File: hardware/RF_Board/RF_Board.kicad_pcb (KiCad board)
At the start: 4 copper layers, 90 x 90 mm, 130 parts, among them J1 Conn_Coaxial, J2 Conn_01x04_Male, J3 Conn_Coaxial, J4 Conn_01x04_Male, J5 Conn_01x06_Female, J6 Conn_01x06_Female, J7 Conn_01x06_Female, J8 L77TSAH15SOL2RM8, Q1 2N7002, Q2 2N7002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

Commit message: Finish RF board routing
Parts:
- removed R24, R25, R26, R27, R28, R29: 0, RF_Board_Footprints:R_0603_1608Metric
- added J9: Conn_01x09_Male, RF_Board_Footprints:PinHeader_1x09_P2.54mm_Vertical, F.Cu at (36.9, 22.6)
- D1, D7: footprint RF_Board_Footprints:D_SMB_Handsoldering -> RF_Board_Footprints:SOD882
- D2, D8: footprint RF_Board_Footprints:D_SMB_Handsoldering -> RF_Board_Footprints:D_SOD-523
- Q1, Q2: footprint RF_Board_Footprints:SOT-23-3 -> Package_TO_SOT_SMD:SOT-23
- moved D8 115.5 mm to (37.5, 54.4)
- moved D1 114.4 mm to (49.9, 57.9)
- moved D7 89.6 mm to (39.9, 57.9)
- moved D2 86.3 mm to (47.4, 54.4)
- moved R6 6.91 mm to (32.9, 50.8), turned to 180 degrees
- moved R7 5.76 mm to (42.8, 50.8), turned to 180 degrees
- moved R16 4.77 mm to (64.9, 62.3), turned to -90 degrees
- moved Q1 4.16 mm to (68.0, 63.1), turned to 180 degrees
- moved D5 2.00 mm to (67.5, 60.3), turned to 180 degrees
- moved R22 1.46 mm to (34.3, 59.1)
- moved C53 1.33 mm to (37.8, 52.7)
- moved C50 1.04 mm to (47.7, 52.7)
- moved D6 0.99 mm to (7.33, 76.0)
- moved Q2 0.99 mm to (6.99, 73.0)
- moved R17 0.99 mm to (9.88, 74.0)
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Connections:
- U10 pad 9: (no net) -> GND
- U11 pad 9: (no net) -> GND
- U14 pad V: (no net) -> GND
- U15 pad V: (no net) -> GND
- U2 pad 1: /CC2500_RX_EMPTY -> /CC2500_TX_EMPTY
- U2 pad 2: /CC2500_TX_OVERFLOW -> /CC2500_RX_OVERFLOW
- U2 pad 3: /CC2500_RX_OVERFLOW -> /CC2500_TX_OVERFLOW
- U2 pad 48: /CC2500_TX_EMPTY -> /CC2500_RX_EMPTY
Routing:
- net /RFM_AUX_RST: track 0.00 -> 74.9 mm, vias 0 -> 1
- net /RFM_AUX_CSN: track 0.00 -> 73.9 mm, vias 0 -> 1
- net /RFM_AUX_DIO0: track 0.00 -> 66.7 mm, vias 0 -> 2
- net /CC2500_CSN: track 24.7 -> 84.2 mm, vias 0 -> 1
- net /GDO0: track 38.5 -> 95.1 mm, vias 0 -> 1
- net /GDO2: track 41.0 -> 95.4 mm, vias 2 -> 3
- net /PA_EN: track 2.44 -> 55.1 mm, vias 1 -> 2
- net /CC2500_MOSI: track 36.0 -> 87.8 mm, vias 2 -> 3
- net /CC2500_MISO: track 31.4 -> 79.6 mm, vias 2 -> 3
- net /PA_VDET: track 6.22 -> 53.2 mm, vias 1 -> 2
- net /CC2500_SCLK: track 34.4 -> 80.4 mm, vias 2 -> 3
- net /3V3_IN: track 0.00 -> 25.6 mm
- net Net-(H3-Pad1): track 0.00 -> 6.68 mm
- net Net-(H2-Pad1): track 0.00 -> 6.68 mm
- net Net-(H4-Pad1): track 0.00 -> 6.67 mm
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- added copper zone on F.Cu, net +3.3V
- added copper zone on In2.Cu, net +3.3V
- added copper zone on F.Cu, net +5V
- added copper zone on In2.Cu, net +5V
- added copper zone on F.Cu, net /3V3_IN
- added copper zone on F.Cu, net /5V0_IN
- added copper zone on B.Cu, net GND
- added copper zone on F.Cu, net GND
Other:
- board text added: "0"
- board text added: "1"
- board text added: "2"
- board text added: "3"
- board text added: "4"
- board text added: "5"
- board text added: "5V"
- board text added: "CSN"
- board text added: "DIO"
- board text added: "GDO0"
- board text added: "GDO2"
- board text added: "MISO"
- board text added: "MOSI"
- board text added: "R'Sat RF Board Rev. 1 Merrick Slane - 2023"
- board text added: "RST"
- board text added: "SBAND"
- board text added: "SBAND ACTY"
- board text added: "SCK"
- board text added: "UHF ACTY"
- board text added: "U_CSN"
- board text added: "U_DIO0"
- board text added: "U_RST"

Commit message: more RF board touch-ups
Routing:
- net +3.3V: vias 17 -> 16
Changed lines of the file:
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@@
   (gr_line (start 88 21) (end 87 21) (layer "B.SilkS") (width 0.15))
   (gr_line (start 88 31) (end 87 31) (layer "B.SilkS") (width 0.15))
+  (gr_line (start 29.718 59.966) (end 29.718 64.03) (layer "F.SilkS") (width 0.15))
+  (gr_line (start 29.718 65.024) (end 29.718 69.088) (layer "F.SilkS") (width 0.15))
   (gr_arc (start 87.46 0) (mid 89.256051 0.743949) (end 90 2.54) (layer "Edge.Cuts") (width 0.2))
   (gr_line (start 87.46 90) (end 2.54 90) (layer "Edge.Cuts") (width 0.2))
@@
   (gr_line (start 2.54 0) (end 87.46 0) (layer "Edge.Cuts") (width 0.2))
   (gr_arc (start 0 2.54) (mid 0.743949 0.743949) (end 2.54 0) (layer "Edge.Cuts") (width 0.2))
+  (gr_text "5V" (at 30.734 67.056 90) (layer "F.SilkS")
+    (effects (font (size 1 1) (thickness 0.2)))
+  )
   (gr_text "SCK" (at 2.032 30.248) (layer "F.SilkS")
     (effects (font (size 1 1) (thickness 0.2)))
@@
     (effects (font (size 1 1) (thickness 0.15)))
   )
+  (gr_text "GND" (at 30.734 61.998 90) (layer "F.SilkS")
+    (effects (font (size 1 1) (thickness 0.2)))
+  )
   (gr_text "U_DIO0" (at 41.529 27.708) (layer "F.SilkS")
     (effects (font (size 1 1) (thickness 0.2)))
@@
     (effects (font (size 1 1) (thickness 0.2)))
   )
-  (segment (start 56.358 49.7078) (end 56.358 48.498) (width 0.3302) (layer "F.Cu") (net 1))
   (segment (start 55.358 47.498) (end 53.467 47.498) (width 0.3302) (layer "F.Cu") (net 1))
   (segment (start 53.058 47.498) (end 53.467 47.498) (width 0.62) (layer "F.Cu") (net 1))
+  (segment (start 56.358 49.7078) (end 56.358 48.498) (width 0.4318) (layer "F.Cu") (net 1))
   (arc (start 56.358 48.498) (mid 56.065107 47.790893) (end 55.358 47.498) (width 0.3302) (layer "F.Cu") (net 1))
   (segment (start 50.2252 47.498) (end 51.562 47.498) (width 0.3302) (layer "F.Cu") (net 2))
@@
   (arc (start 50.2252 47.498) (mid 49.518093 47.205107) (end 49.2252 46.498) (width 0.3302) (layer "F.Cu") (net 2))
   (segment (start 68.834 42.87) (end 68.834 43.434) (width 0.62) (layer "F.Cu") (net 3))
-  (segment (start 58.307998 49.7078) (end 58.307998 48.228) (width 0.3302) (layer "F.Cu") (net 3))
+  (segment (start 58.307998 49.7078) (end 58.307998 48.228) (width 0.4318) (layer "F.Cu") (net 3))
   (segment (start 60.307998 46.228) (end 66.834 46.228) (width 0.3302) (layer "F.Cu") (net 3))
   (segment (start 68.834 44.228) (end 68.834 43.434) (width 0.3302) (layer "F.Cu") (net 3))
@@
   (via (at 55.109 36.957) (size 0.508) (drill 0.254) (layers "F.Cu" "B.Cu") (net 14))
   (via (at 15.876 14.478) (size 1) (drill 0.5) (layers "F.Cu" "B.Cu") (net 14))
-  (via (at 36.83 52.705) (size 0.508) (drill 0.254) (layers "F.Cu" "B.Cu") (net 14))
+  (via (at 36.83 52.705) (size 1) (drill 0.5) (layers "F.Cu" "B.Cu") (net 14))
   (via (at 75.946 40.386) (size 1) (drill 0.5) (layers "F.Cu" "B.Cu") (net 14))
-  (via (at 36.83 50.8) (size 0.508) (drill 0.254) (layers "F.Cu" "B.Cu") (net 14))
+  (via (at 36.83 50.8) (size 1) (drill 0.5) (layers "F.Cu" "B.Cu") (net 14))
   (via (at 75.946 34.036) (size 1) (drill 0.5) (layers "F.Cu" "B.Cu") (net 14))
   (via (at 53.848 33.02) (size 1) (drill 0.5) (layers "F.Cu" "B.Cu") (net 14))
@@
   (via (at 46.736 50.8) (size 0.508) (drill 0.254) (layers "F.Cu" "B.Cu") (net 22))
   (via (at 80.455 55.626) (size 0.508) (drill 0.254) (layers "F.Cu" "B.Cu") (net 22))
-  (via (at 73.66 62.738) (size 1.016) (drill 0.508) (layers "F.Cu" "B.Cu") (net 22))
   (via (at 53.848 70.358) (size 0.508) (drill 0.254) (layers "F.Cu" "B.Cu") (net 22))
   (via (at 59.944 67.3625) (size 0.508) (drill 0.254) (layers "F.Cu" "B.Cu") (free) (net 22))
@@
   (via (at 6.5475 75.971) (size 0.508) (drill 0.254) (layers "F.Cu" "B.Cu") (net 22))
   (via (at 78.677 58.674) (size 0.508) (drill 0.254) (layers "F.Cu" "B.Cu") (net 22))
-  (via (at 46.736 52.705) (size 0.508) (drill 0.254) (layers "F.Cu" "B.Cu") (net 22))
+  (via (at 46.736 52.705) (size 1) (drill 0.5) (layers "F.Cu" "B.Cu") (net 22))
   (via (at 52.578 65.278) (size 1) (drill 0.5) (layers "F.Cu" "B.Cu") (net 22))
-  (via (at 73.66 62.738) (size 1.016) (drill 0.508) (layers "F.Cu" "B.Cu") (net 22))
+  (via (at 73.66 62.738) (size 1) (drill 0.5) (layers "F.Cu" "B.Cu") (net 22))
   (via (at 61.497476 69.058524) (size 0.508) (drill 0.254) (layers "F.Cu" "B.Cu") (free) (net 22))
   (via (at 46.736 54.356) (size 0.508) (drill 0.254) (layers "F.Cu" "B.Cu") (net 22))

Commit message: more RF board touch-ups
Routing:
- net /PA_VDET: track 53.2 -> 59.0 mm
- net /RFM_AUX_RST: track 74.9 -> 78.8 mm
- net /RFM_AUX_CSN: track 73.9 -> 77.8 mm
- net /LNA_BP_A: track 30.9 -> 32.9 mm
- net /LNA_BP_B: track 36.3 -> 37.6 mm
- net /PA_EN: track 55.1 -> 56.4 mm
- net GND: vias 11 -> 131
- net +5V: vias 11 -> 14
- added copper zone on F.Cu, net Net-(J3-Pad1)
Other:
- board text added: "Board ordering specifications: -1oz outer copper/0.5oz inner copper -50ohm trace width appoximately 13mil -Epoxy filled and capped vias"
- board text added: "Board ordering specifications: -1oz outer copper/0.5oz inner copper -50ohm trace width appoximately 13mil -Vias must be epoxy-filled and copper capped with soldermask coverage when not in-pad"

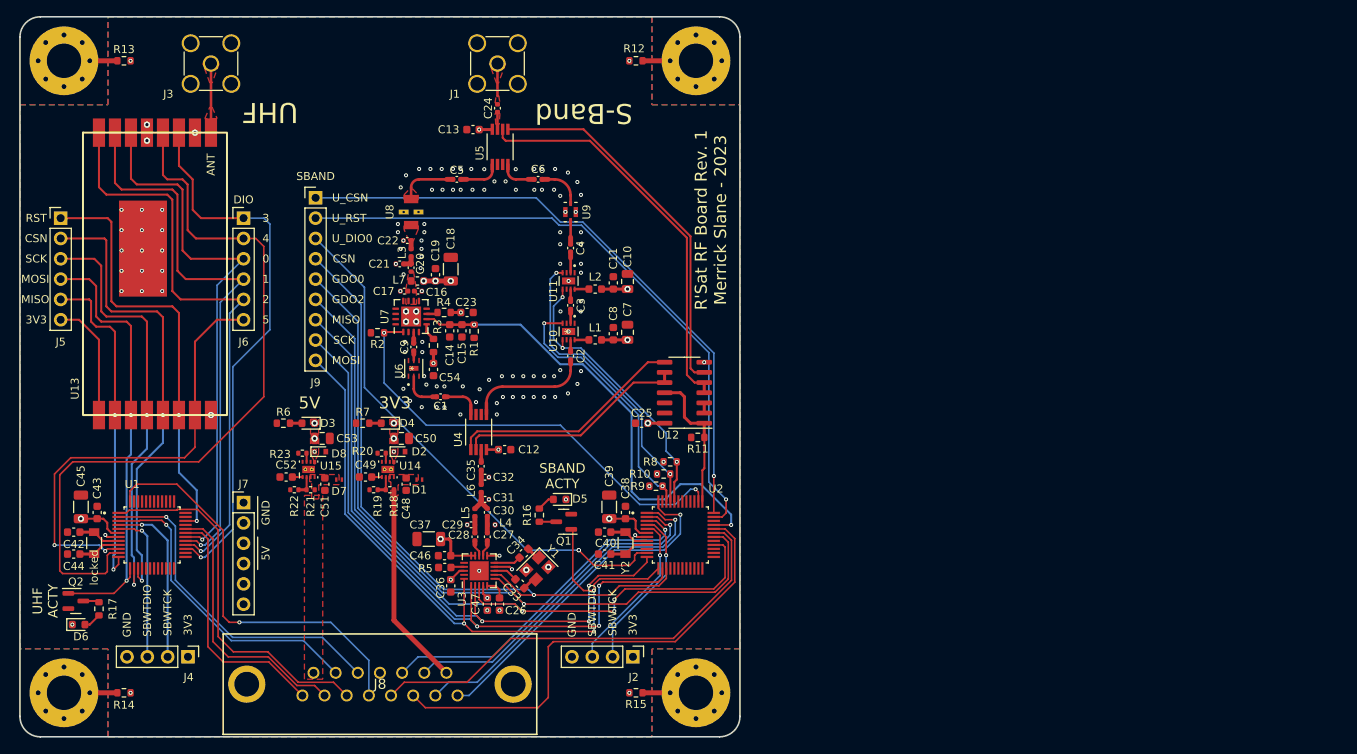
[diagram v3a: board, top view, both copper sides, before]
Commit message: finished RF board layout, sending to review
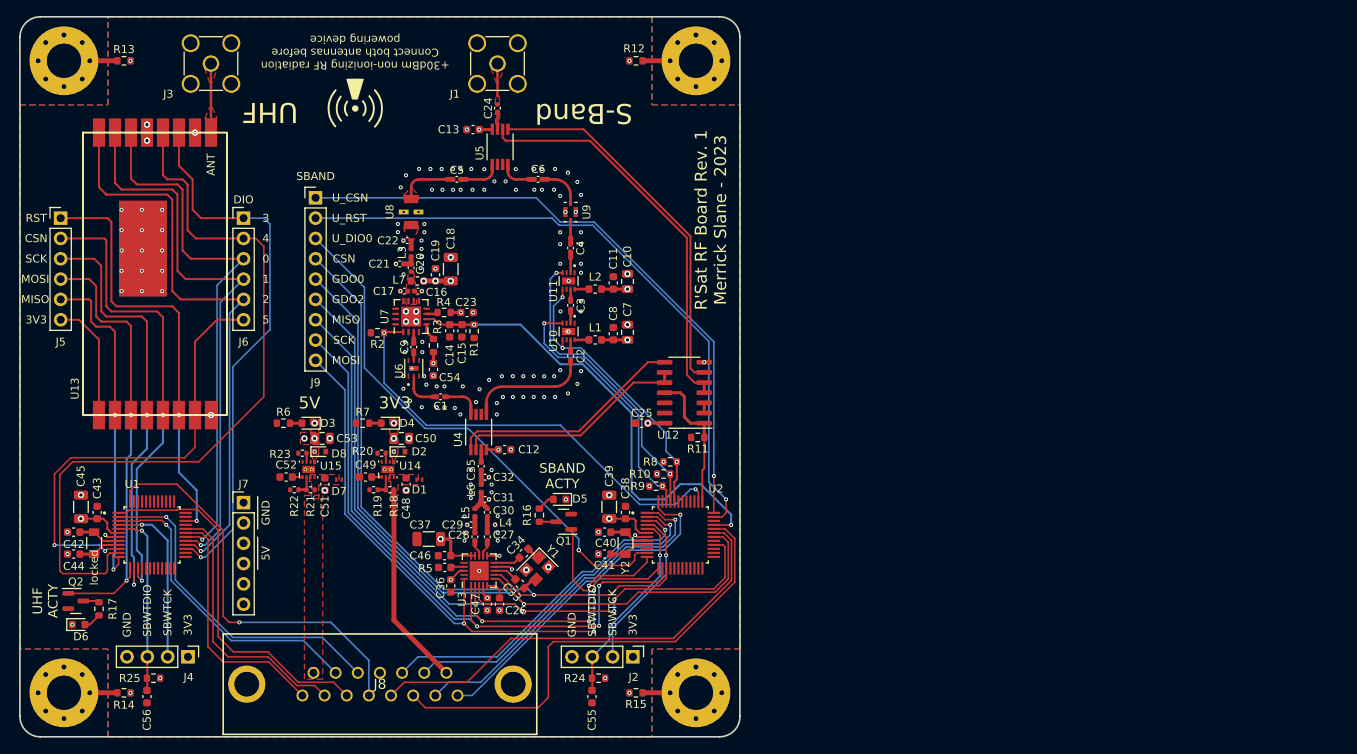
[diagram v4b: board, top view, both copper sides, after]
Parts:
- added C55: 1nF, RF_Board_Footprints:C_0603_1608Metric, F.Cu at (71.5, 85.0)
- added C56: 1nF, RF_Board_Footprints:C_0603_1608Metric, F.Cu at (15.9, 85.0)
- added G***: LOGO, RF_Board_Footprints:RF_notice, F.Cu at (41.9, 10.8)
- added R24: 47k, RF_Board_Footprints:R_0603_1608Metric, F.Cu at (72.3, 82.7)
- added R25: 47k, RF_Board_Footprints:R_0603_1608Metric, F.Cu at (16.7, 82.7)
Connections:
- U14 pad V: GND -> (no net)
- U15 pad V: GND -> (no net)
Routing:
- net /CC2500_SBWTDIO: track 20.7 -> 25.0 mm
- net /RFM_SBWTDIO: track 19.1 -> 23.3 mm
- net /RFM_AUX_RST: track 78.8 -> 79.6 mm
- net /RFM_AUX_CSN: track 77.8 -> 78.6 mm
- net /RFM_AUX_DIO0: track 66.7 -> 66.1 mm
- net GND: vias 131 -> 163
- net +5V: vias 14 -> 15
- net +3.3V: vias 16 -> 18
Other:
- board text added: "+30dBm non-ionizing RF radiation Connect both antennas before powering device"
- board text added: "Board ordering specifications: -1oz outer copper/0.5oz inner copper -50ohm trace width appoximately 13mil -Vias must be epoxy filled and copper capped"
- board text added: "Software for this board can be found at: https://github.com/jbrown3859/EE175-SeniorDesign Program MCUs through J2 and J4 with a compatible TI eZ-FET debug probe"
- board text removed: "Board ordering specifications: -1oz outer copper/0.5oz inner copper -50ohm trace width appoximately 13mil -Vias must be epoxy-filled and copper capped with soldermask coverage when not in-pad"

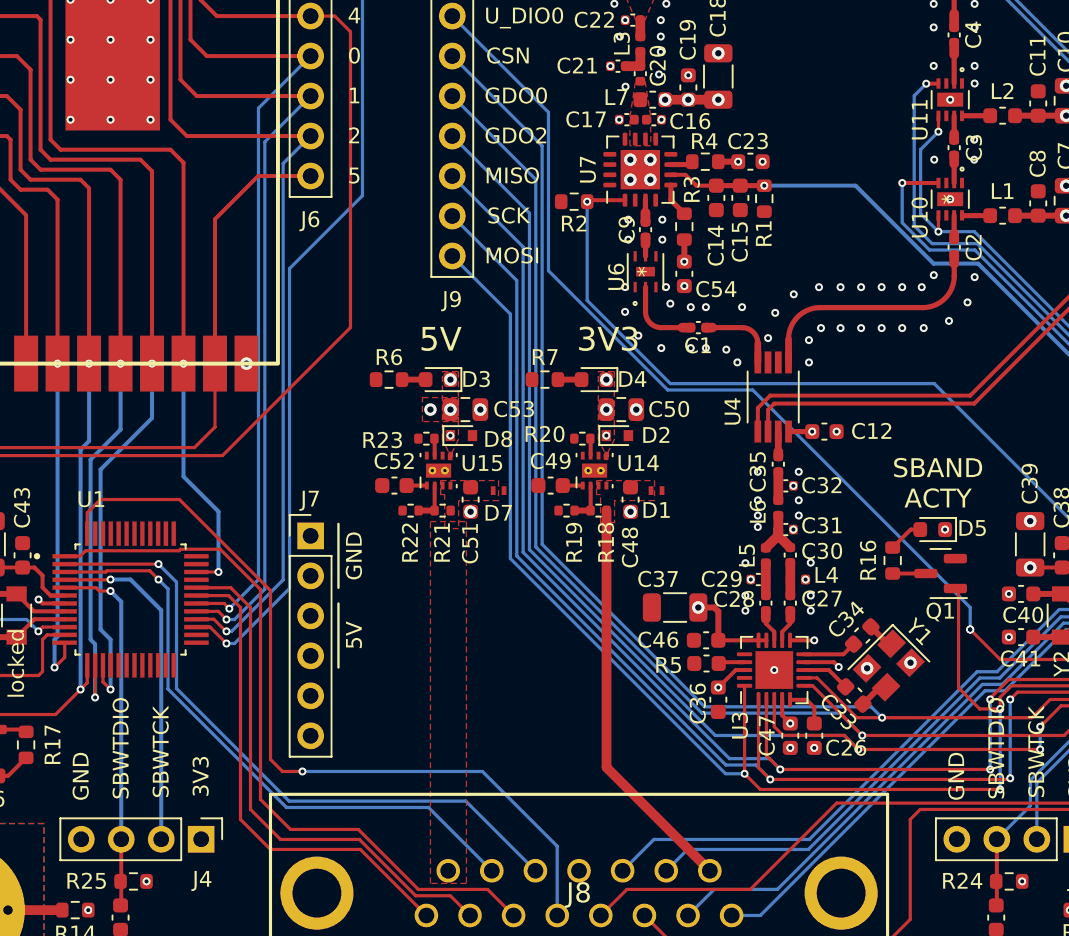
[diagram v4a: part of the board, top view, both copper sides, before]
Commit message: resolve DRC errors
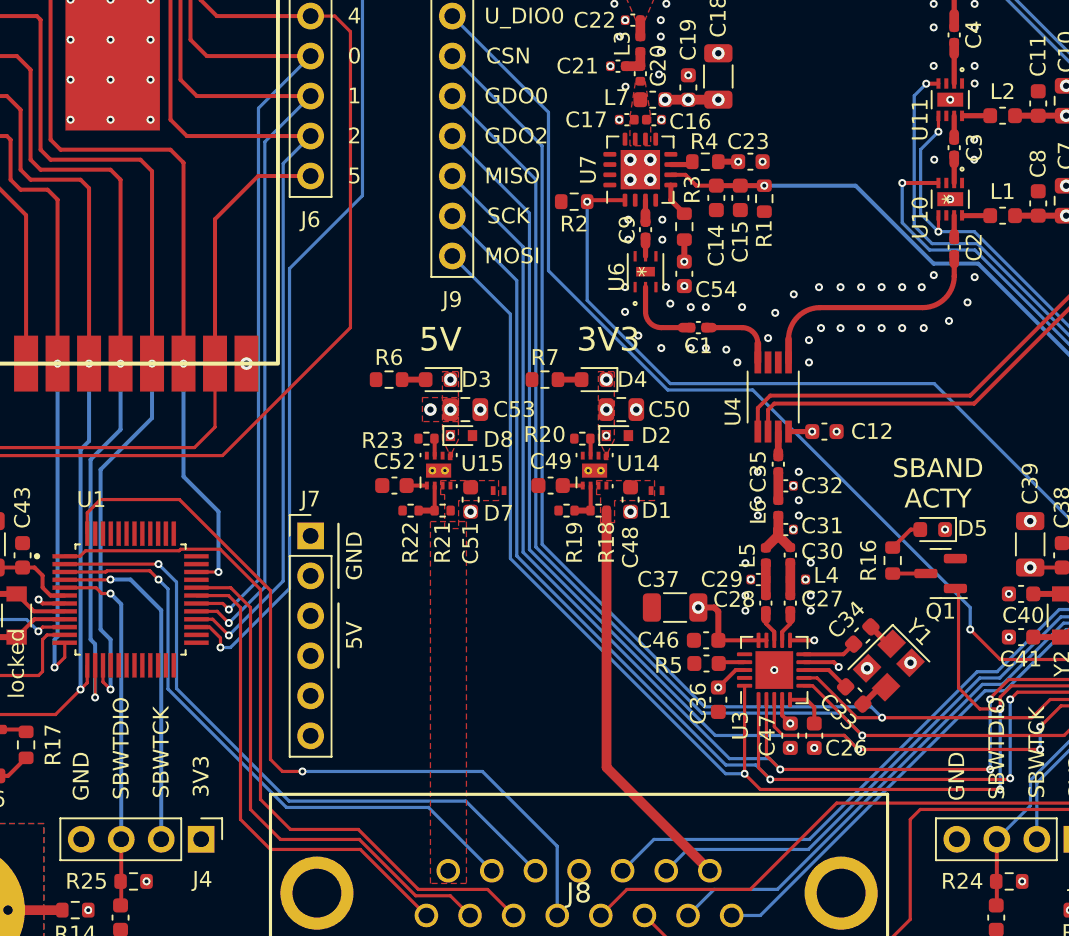
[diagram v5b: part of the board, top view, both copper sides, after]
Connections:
- U14 pad V: (no net) -> GND
- U15 pad V: (no net) -> GND
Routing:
- net /RFM_DIO3: track 68.6 -> 69.2 mm
- net GND: vias 163 -> 162
- net /RFM_AUX_DIO0: vias 2 -> 1
